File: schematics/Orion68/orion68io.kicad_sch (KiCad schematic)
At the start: 0 parts

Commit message: Schematics update
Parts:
- added C1: 100uF, symbol Device:C_Polarized
- added D5: LED, symbol Device:LED
- added J10: Euro96pin, ConnPdSilva:conn_euro96, symbol ConnPdSilva:ConnEuro96
- added J200: DB25_Socket, symbol Connector:DB25_Socket
- added J6: IDE, symbol Connector_Generic:Conn_02x20_Odd_Even
- added J7: sdcard, symbol Connector_Generic:Conn_01x06
- added J8: RTC, symbol Connector_Generic:Conn_01x06
- added LS1: Speaker, symbol Device:Speaker
- added Q4: NPN, symbol Simulation_SPICE:NPN
- added R17, R20, R21, R22, R23, R24, R25, R26, R27, R28, R29, R30, R31: 1k, symbol Device:R
- added R18, R19: 4k7, symbol Device:R
- added R32: 1K, symbol Device:R
- added R33: 47R, symbol Device:R
- added U14: 8253, Package_DIP:DIP-24_W15.24mm, symbol Timer:8253
- added U15: Multio, symbol pdSilva:Raspi pi pico
- added U16, U17: 74HC245, symbol 74xx:74HC245
- added U200: GAL16V8, symbol Logic_Programmable:GAL16V8
- added U200: PAL20RS10, Package_DIP:DIP-24_W7.62mm, symbol Logic_Programmable:PAL20RS10
- added U201: 82C55A, Package_DIP:DIP-40_W15.24mm, symbol Interface:82C55A
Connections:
- new net: U15.1 (GP0), U16.2 (A0)
- new net: U15.10 (GP7), U16.9 (A7)
- new net: U15.11 (GP8), U17.2 (A0)
- new net: U15.12 (GP9), U17.3 (A1)
- new net: U15.14 (GP10), U17.4 (A2)
- new net: U15.15 (GP11), U17.5 (A3)
- new net: U15.2 (GP1), U16.3 (A1)
- new net: U15.4 (GP2), U16.4 (A2)
- new net: U15.5 (GP3), U16.5 (A3)
- new net: U15.6 (GP4), U16.6 (A4)
- new net: U15.7 (GP5), U16.7 (A5)
- new net: U15.9 (GP6), U16.8 (A6)
- new net: C1.1, Q4.1 (C), R33.2
- new net: C1.2, LS1.1
- new net: R31.2, U17.15 (B3)
- new net: R21.2, U16.17 (B1)
- new net: D5.1 (K), R17.1
- new net: Q4.2 (B), R32.2
- new net: R30.2, U17.16 (B2)
- new net: R29.2, U17.17 (B1)
- new net: R24.2, U16.14 (B4)
- new net: R27.2, U16.11 (B7)
- new net: R20.2, U16.18 (B0)
- new net: R22.2, U16.16 (B2)
- new net: R28.2, U17.18 (B0)
- new net: R26.2, U16.12 (B6)
- new net: R25.2, U16.13 (B5)
- new net: R23.2, U16.15 (B3)
- new net +12V: J10.92
- new net +5V: D5.2 (A), J10.1, J10.33, J10.65, J6.38 (Pin_38), J7.2 (Pin_2), R18.1, R19.1, R33.1, U14.24 (VCC), U200.20 (VCC), U200.24 (VCC), U201.26 (VCC)
- new net -5V: J10.94
- new net 3V3_from_sdcard: U15.39 (VSYS), U16.20 (VCC), U17.20 (VCC)
- new net ALE: J10.73
- new net BA0: J10.18
- new net BA06: U200.1 (I1/CLK), U200.2 (I0)
- new net BA07: U200.2 (I2), U200.3 (I1)
- new net BA08: U200.3 (I3), U200.4 (I2)
- new net BA09: U200.4 (I4), U200.5 (I3)
- new net BA0A: U200.5 (I5), U200.6 (I4)
- new net BA0B: U200.6 (I6), U200.7 (I5)
- new net BA1: J10.19, J6.35 (Pin_35), R28.1, U14.19 (A0), U201.9 (A0)
- new net BA10: J10.28
- new net BA11: J10.29
- new net BA12: J10.30
- new net BA13: J10.31
- new net BA14: J10.63
- new net BA15: J10.62
- new net BA16: J10.61
- new net BA17: J10.60
- new net BA18: J10.59
- new net BA19: J10.58
- new net BA2: J10.20, J6.33 (Pin_33), R29.1, U14.20 (A1), U201.8 (A1)
- new net BA20: J10.57
- new net BA21: J10.56
- new net BA22: J10.55
- new net BA23: J10.54
- new net BA3: J10.21, J6.36 (Pin_36), R30.1
- new net BA4: J10.22, R31.1
- new net BA5: J10.23
- new net BA6: J10.24
- new net BA7: J10.25
- new net BA8: J10.26
- new net BA9: J10.27
- new net BD0: J10.2, J6.4 (Pin_4), R20.1, U14.8 (D0), U201.34 (D0)
- new net BD1: J10.3, J6.6 (Pin_6), R21.1, U14.7 (D1), U201.33 (D1)
- new net BD10: J10.12, J6.7 (Pin_7)
- new net BD11: J10.13, J6.9 (Pin_9)
- new net BD12: J10.14, J6.11 (Pin_11)
- new net BD13: J10.15, J6.13 (Pin_13)
- new net BD14: J10.16, J6.15 (Pin_15)
- new net BD15: J10.17, J6.17 (Pin_17)
- new net BD2: J10.4, J6.8 (Pin_8), R22.1, U14.6 (D2), U201.32 (D2)
- new net BD3: J10.5, J6.10 (Pin_10), R23.1, U14.5 (D3), U201.31 (D3)
- new net BD4: J10.6, J6.12 (Pin_12), R24.1, U14.4 (D4), U201.30 (D4)
- new net BD5: J10.7, J6.14 (Pin_14), R25.1, U14.3 (D5), U201.29 (D5)
- new net BD6: J10.8, J6.16 (Pin_16), R26.1, U14.2 (D6), U201.28 (D6)
- new net BD7: J10.9, J6.18 (Pin_18), R27.1, U14.1 (D7), U201.27 (D7)
- new net BD8: J10.10, J6.3 (Pin_3)
- new net BD9: J10.11, J6.5 (Pin_5)
- new net BOOTIN: J10.87
- new net BUSY: J200.11, U201.15 (PC1)
- new net B/cpurd: J10.45, J6.25 (Pin_25), U14.22 (~{RD}), U200.1 (CLK), U200.12 (IO8), U201.5 (~{RD})
- new net B/cpurw: J10.46, J6.23 (Pin_23), U14.23 (~{WR}), U200.13 (IO7), U200.13 (~{OE}), U201.36 (~{WR})
- new net CPU_CLK: J10.81
- new net CRUCLK: J10.35
- new net CRUIN: J10.36
- new net CRUOUT: J10.37
- new net CS: J7.6 (Pin_6), U15.22 (GP17)
- new net CS_82C55: U201.6 (~{CS})
- new net CS_TIMER: U14.21 (~{CS})
- new net D0: J200.2, U201.4 (PA0)
- new net D1: J200.3, U201.3 (PA1)
- new net D2: J200.4, U201.2 (PA2)
- new net D3: J200.5, U201.1 (PA3)
- new net D4: J200.6, U201.40 (PA4)
- new net D5: J200.7, U201.39 (PA5)
- new net D6: J200.8, U201.38 (PA6)
- new net D7: J200.9, U201.37 (PA7)
- new net DBIN: J10.38
- new net DMARQ: J6.21 (Pin_21)
- new net DS: J8.2 (Pin_2)
- new net DT/R: J10.75
- new net E: J10.34
- new net GND: J10.32, J10.64, J10.93, J10.95, J10.96, J200.18 (P18), J200.19 (P19), J200.20 (P20), J200.21 (P21), J200.22 (P22), J200.23 (P23), J200.24 (P24), J200.25 (P25), J6.19 (Pin_19), J6.2 (Pin_2), J6.22 (Pin_22), J6.24 (Pin_24), J6.26 (Pin_26), J6.28 (Pin_28), J6.30 (Pin_30), J6.40 (Pin_40), J7.1 (Pin_1), J8.6 (Pin_6), LS1.2, Q4.3 (E), U14.12 (GND), U15.13 (GND), U15.18 (GND), U15.23 (GND), U15.28 (GND), U15.3 (GND), U15.33 (GND), U15.38 (GND), U15.8 (GND), U16.1 (A->B), U16.10 (GND), U16.19 (CE), U17.1 (A->B), U17.10 (GND), U17.11 (B7), U17.12 (B6), U17.13 (B5), U17.14 (B4), U17.19 (CE), U200.10 (GND), U200.12 (GND), U201.7 (GND)
- new net HLDA: J10.52
- new net IAQ: J10.39
- new net IC3: J10.47
- new net INTRQ: J6.31 (Pin_31)
- new net IORDY: J6.27 (Pin_27)
- new net IRQ2: J10.48
- new net IRQ3: J10.49
- new net IRQ4: J10.50
- new net IRQ5: J10.89
- new net IRQ6: J10.90
- new net IRQ7: J10.91
- new net MISO: J7.3 (Pin_3), U15.21 (GP16)
- new net MOSI: J7.4 (Pin_4), U15.25 (GP19)
- new net M/IO: J10.76
- new net NMI: J10.41
- new net PWR_GOOD: J10.88
- new net RDY: J10.44
- new net RESET: J10.67, U201.35 (RESET)
- new net Res9: J10.69
- new net SCK: J7.5 (Pin_5), U15.24 (GP18)
- new net SCL: J8.3 (Pin_3), R18.2, U15.32 (GP27)
- new net SDA: J8.4 (Pin_4), R19.2, U15.31 (GP26)
- new net SQ: J8.1 (Pin_1)
- new net STROBE: J200.1, U201.14 (PC0)
- new net TICK_IN: J10.86, U15.34 (GP28)
- new net Vcc: J8.5 (Pin_5)
- new net audio: R32.1, U15.29 (GP22)
- new net /AS: J10.43
- new net /BAS: U200.7 (I7), U200.8 (I6)
- new net /BERR: J10.68
- new net /BLDS: U200.8 (I8), U200.9 (I7)
- new net /BUDS: U200.10 (I8), U200.9 (I9)
- new net /CS_82C55: U200.19 (IO1), U200.23 (O0)
- new net /CS_IDE: J6.37 (Pin_37), U200.18 (IO2), U200.22 (O1)
- new net /CS_MULTIO: U15.26 (GP20), U200.15 (IO5)
- new net /CS_RTC: U200.17 (I03), U200.21 (O2)
- new net /CS_SDCARD: U200.19 (O4)
- new net /CS_TIMER: U200.16 (IO4), U200.20 (O3)
- new net /DASP: J6.39 (Pin_39), R17.2
- new net /DEN: J10.74
- new net /DMACK: J6.29 (Pin_29)
- new net /HALT: J10.53
- new net /HOLD: J10.42
- new net /INTA: J10.72
- new net /INTR: J10.40
- new net /IOCS16: J6.32 (Pin_32)
- new net /IO_CS: J10.85, U200.11 (I10/~{OE}), U200.11 (I9)
- new net /LDS: J10.70
- new net /M1: J10.79
- new net /PDIAG: J6.34 (Pin_34)
- new net /RD: U15.17 (GP13)
- new net /RESET: J10.66, J6.1 (Pin_1)
- new net /RFSH: J10.80
- new net /RST: J10.51
- new net /SSO: J10.77
- new net /UDS: J10.71
- new net /WAIT: J10.78
- new net /WR: U15.16 (GP12)
- no-connect marks 0 -> 6
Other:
- note added: "+-----------------------------+-------------------+ |Sinal SPI,SPI0 (Opção Padrão)|SPI1 (Opção Padrão)| |RX (MISO),GP16 (Pino 21) |GP12 (Pino 16) | |CSn (CS), GP17 (Pino 22) |GP13 (Pino 17) | |SCK (CLK), GP18 (Pino 24) |GP14 (Pino 19) | |TX (MOSI),GP19 (Pino 25) |GP15 (Pino 20) | +-----------------------------+-------------------+"
- note added: "0xF00040-0xF0007F -> 82C55 0xF00080-0xF000BF -> IDE 0xF000C0-0xF000FF -> RTC 0xF00140-0xF0017F -> TIMER 0xF00180-0xF001BF -> SDCARD 0xF001C0-0xF001FF -> free 0xF00240-0xF0027F -> free 0xF00280-0xF002BF -> free 0xF002C0-0xF002FF -> free 0xF00340-0xF0037F -> free"
- note added: "DB25 fêmea +-------+--------------+--------------+---------------------------------------------+ |Pino |,Nome |,Direção (PC) |,Função | +-------+--------------+--------------+---------------------------------------------+ |1 |,Strobe |,Saída |,Indica que os dados são válidos (Ativo em 0)| |2 |,D0 |,E/S |,Bit de Dados 0 (LSB) | |3 |,D1 |,E/S |,Bit de Dados 1 | |4 |,D2 |,E/S |,Bit de Dados 2 | |5 |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"

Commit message: Schematics update
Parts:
- U15: footprint (none) -> Package_DIP:DIP-40_W15.24mm
- renumbered U200 to U9999
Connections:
- net /CS_SDCARD: now also U200.14 (IO6); no longer U9999.19 (O4)
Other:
- moved on the sheet: U9999
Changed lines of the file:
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@@
 	)
 	(label "BA0A"
-		(at 64.77 254 180)
+		(at 66.04 311.15 180)
 		(effects
 			(font
@@
 	)
 	(label "{slash}BLDS"
-		(at 64.77 261.62 180)
+		(at 66.04 318.77 180)
 		(effects
 			(font
@@
 	)
 	(label "{slash}IO_CS"
-		(at 64.77 266.7 180)
+		(at 66.04 323.85 180)
 		(effects
 			(font
@@
 	)
 	(label "{slash}BAS"
-		(at 64.77 259.08 180)
+		(at 66.04 316.23 180)
 		(effects
 			(font
@@
 	)
 	(label "{slash}CS_IDE"
-		(at 90.17 246.38 0)
+		(at 91.44 303.53 0)
 		(effects
 			(font
@@
 	)
 	(label "BA09"
-		(at 64.77 251.46 180)
+		(at 66.04 308.61 180)
 		(effects
 			(font
@@
 	)
 	(label "BA0B"
-		(at 64.77 256.54 180)
+		(at 66.04 313.69 180)
 		(effects
 			(font
@@
 	)
 	(label "BA07"
-		(at 64.77 246.38 180)
+		(at 66.04 303.53 180)
 		(effects
 			(font
@@
 	)
 	(label "{slash}BUDS"
-		(at 64.77 264.16 180)
+		(at 66.04 321.31 180)
 		(effects
 			(font
@@
 	)
 	(label "BA08"
-		(at 64.77 248.92 180)
+		(at 66.04 306.07 180)
 		(effects
 			(font
@@
 	)
 	(label "{slash}CS_SDCARD"
-		(at 90.17 254 0)
+		(at 45.72 260.35 0)
 		(effects
 			(font
@@
 	)
 	(label "BA06"
-		(at 64.77 243.84 180)
+		(at 66.04 300.99 180)
 		(effects
 			(font
@@
 	)
 	(label "{slash}CS_RTC"
-		(at 90.17 248.92 0)
+		(at 91.44 306.07 0)
 		(effects
 			(font
@@
 	)
 	(label "B{slash}cpurw"
-		(at 64.77 274.32 180)
+		(at 66.04 331.47 180)
 		(effects
 			(font
@@
 	)
 	(label "B{slash}cpurd"
-		(at 64.77 271.78 180)
+		(at 66.04 328.93 180)
 		(effects
 			(font
@@
 	)
 	(label "{slash}CS_82C55"
-		(at 90.17 243.84 0)
+		(at 91.44 300.99 0)
 		(effects
 			(font
@@
 	)
 	(label "{slash}CS_TIMER"
-		(at 90.17 251.46 0)
+		(at 91.44 308.61 0)
 		(effects
 			(font
@@
 			)
 		)
-		(property "Footprint" ""
+		(property "Footprint" "Package_DIP:DIP-40_W15.24mm"
 			(at 199.39 104.14 0)
 			(effects
@@
 	(symbol
 		(lib_id "power:GND")
-		(at 77.47 279.4 0)
+		(at 78.74 336.55 0)
 		(unit 1)
 		(exclude_from_sim no)
@@
 		(fields_autoplaced yes)
 		(property "Reference" "#PWR085"
-			(at 77.47 285.75 0)
+			(at 78.74 342.9 0)
 			(effects
 				(font
@@
 		)
 		(property "Value" "GND"
-			(at 77.47 284.48 0)
+			(at 78.74 341.63 0)
 			(effects
 				(font
@@
 		)
 		(property "Footprint" ""
-			(at 77.47 279.4 0)
+			(at 78.74 336.55 0)
 			(effects
 				(font
@@
 		)
 		(property "Datasheet" ""
-			(at 77.47 279.4 0)
+			(at 78.74 336.55 0)
 			(effects
 				(font
@@
 		)
 		(property "Description" "Power symbol creates a global label with name \"GND\" , ground"
-			(at 77.47 279.4 0)
+			(at 78.74 336.55 0)
 			(effects
 				(font
@@
 	(symbol
 		(lib_id "power:+5V")
-		(at 77.47 238.76 0)
+		(at 78.74 295.91 0)
 		(unit 1)
 		(exclude_from_sim no)
@@
 		(fields_autoplaced yes)
 		(property "Reference" "#PWR090"
-			(at 77.47 242.57 0)
+			(at 78.74 299.72 0)
 			(effects
 				(font
@@
 		)
 		(property "Value" "+5V"
-			(at 77.47 233.68 0)
+			(at 78.74 290.83 0)
 			(effects
 				(font
@@
 		)
 		(property "Footprint" ""
-			(at 77.47 238.76 0)
+			(at 78.74 295.91 0)
 			(effects
 				(font
@@
 		)
 		(property "Datasheet" ""
-			(at 77.47 238.76 0)
+			(at 78.74 295.91 0)
 			(effects
 				(font
@@
 		)
 		(property "Description" "Power symbol creates a global label with name \"+5V\""
-			(at 77.47 238.76 0)
+			(at 78.74 295.91 0)
 			(effects
 				(font
@@
 	(symbol
 		(lib_id "Logic_Programmable:PAL20RS10")
-		(at 77.47 259.08 0)
+		(at 78.74 316.23 0)
 		(unit 1)
 		(exclude_from_sim no)
@@
 		(dnp no)
 		(fields_autoplaced yes)
-		(property "Reference" "U200"
-			(at 79.6133 237.49 0)
+		(property "Reference" "U9999"
+			(at 80.8833 294.64 0)
 			(effects
 				(font
@@
 		)
 		(property "Value" "PAL20RS10"
-			(at 79.6133 240.03 0)
+			(at 80.8833 297.18 0)
 			(effects
 				(font
@@
 		)
 		(property "Footprint" "Package_DIP:DIP-24_W7.62mm"
-			(at 77.47 259.08 0)
+			(at 78.74 316.23 0)
 			(effects
 				(font
@@
 		)
 		(property "Datasheet" ""
-			(at 77.47 259.08 0)
+			(at 78.74 316.23 0)
 			(effects
 				(font
@@
 		)
 		(property "Description" "Programmable Logic Array, DIP-24 (Narrow)"
-			(at 77.47 259.08 0)
+			(at 78.74 316.23 0)
 			(effects
 				(font
@@
 			(project "Orion68"
 				(path "/c7ab032b-c937-44de-ab42-c91dee57f0a8/a3cb64b8-9a58-4dca-a498-ee5e38308bd0"
-					(reference "U200")
+					(reference "U9999")
 					(unit 1)
 				)

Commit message: Updating
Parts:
- removed U14: 8253, Package_DIP:DIP-24_W15.24mm, symbol Timer:8253
- removed U9999: PAL20RS10, Package_DIP:DIP-24_W7.62mm, symbol Logic_Programmable:PAL20RS10
- added R212: 1k, Resistor_THT:R_Axial_DIN0204_L3.6mm_D1.6mm_P5.08mm_Horizontal, symbol Device:R
- C_S400: renamed from C1; footprint (none) -> Capacitor_THT:CP_Radial_D5.0mm_P2.50mm
- D_S300: renamed from D5; footprint (none) -> Diode_THT:D_T-1_P5.08mm_Horizontal
- J_S100: renamed from J200; footprint (none) -> Connector_PinHeader_2.54mm:PinHeader_2x13_P2.54mm_Vertical
- J_S200: renamed from J7; footprint (none) -> Connector_PinSocket_2.54mm:PinSocket_1x06_P2.54mm_Vertical
- J_S201: renamed from J8; footprint (none) -> Connector_PinSocket_2.54mm:PinSocket_1x06_P2.54mm_Vertical
- J_S300: renamed from J6; footprint (none) -> Connector_PinHeader_2.54mm:PinHeader_2x20_P2.54mm_Horizontal
- LS_S400: renamed from LS1; footprint (none) -> Connector_PinHeader_2.54mm:PinHeader_1x02_P2.54mm_Vertical
- Q_S400: renamed from Q4; footprint (none) -> Package_TO_SOT_THT:TO-92L_Inline
- R200: renamed from R20; footprint (none) -> Resistor_THT:R_Axial_DIN0204_L3.6mm_D1.6mm_P5.08mm_Horizontal
- R201: renamed from R21; footprint (none) -> Resistor_THT:R_Axial_DIN0204_L3.6mm_D1.6mm_P5.08mm_Horizontal
- R202: renamed from R22; footprint (none) -> Resistor_THT:R_Axial_DIN0204_L3.6mm_D1.6mm_P5.08mm_Horizontal
- R203: renamed from R23; footprint (none) -> Resistor_THT:R_Axial_DIN0204_L3.6mm_D1.6mm_P5.08mm_Horizontal
- R204: renamed from R24; footprint (none) -> Resistor_THT:R_Axial_DIN0204_L3.6mm_D1.6mm_P5.08mm_Horizontal
- R205: renamed from R25; footprint (none) -> Resistor_THT:R_Axial_DIN0204_L3.6mm_D1.6mm_P5.08mm_Horizontal
- R206: renamed from R26; footprint (none) -> Resistor_THT:R_Axial_DIN0204_L3.6mm_D1.6mm_P5.08mm_Horizontal
- R207: renamed from R27; footprint (none) -> Resistor_THT:R_Axial_DIN0204_L3.6mm_D1.6mm_P5.08mm_Horizontal
- R208: renamed from R28; footprint (none) -> Resistor_THT:R_Axial_DIN0204_L3.6mm_D1.6mm_P5.08mm_Horizontal
- R209: renamed from R29; footprint (none) -> Resistor_THT:R_Axial_DIN0204_L3.6mm_D1.6mm_P5.08mm_Horizontal
- R210: renamed from R30; footprint (none) -> Resistor_THT:R_Axial_DIN0204_L3.6mm_D1.6mm_P5.08mm_Horizontal
- R211: renamed from R31; footprint (none) -> Resistor_THT:R_Axial_DIN0204_L3.6mm_D1.6mm_P5.08mm_Horizontal
- R213: renamed from R18; footprint (none) -> Resistor_THT:R_Axial_DIN0204_L3.6mm_D1.6mm_P5.08mm_Horizontal
- R214: renamed from R19; footprint (none) -> Resistor_THT:R_Axial_DIN0204_L3.6mm_D1.6mm_P5.08mm_Horizontal
- R_S300: renamed from R17; footprint (none) -> Resistor_THT:R_Axial_DIN0204_L3.6mm_D1.6mm_P5.08mm_Horizontal
- R_S400: renamed from R33; footprint (none) -> Resistor_THT:R_Axial_DIN0204_L3.6mm_D1.6mm_P5.08mm_Horizontal
- R_S401: renamed from R32; footprint (none) -> Resistor_THT:R_Axial_DIN0204_L3.6mm_D1.6mm_P5.08mm_Horizontal
- U200: footprint (none) -> Package_DIP:DIP-20_W7.62mm
- U_S201: renamed from U16; footprint (none) -> Package_DIP:DIP-20_W7.62mm
- U_S202: renamed from U17; footprint (none) -> Package_DIP:DIP-20_W7.62mm
- renumbered J10 to J200, U201 to U_S100, U15 to U_S200
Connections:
- net BA5: now also R212.1
- net GND: no longer U_S202.14 (B4)
- new net: R212.2, U_S202.14 (B4)
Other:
- note added: "+---------+-----+---------+------------+ |Binário | LDS | Ender. |D0-D7 (LDS)| |A5...A1 | A0 | Decimal |D8-D15 (UDS)| +---------+-----+---------+------------+ |00000 | 0 | 0(Par) | LDS | |00000 | 1 | 1(Ímpar)| UDS | |00001 | 0 | 2(Par) | LDS | |00001 | 1 | 3(Ímpar)| UDS | |00010 | 0 | 4(Par) | LDS | |00010 | 1 | 5(Ímpar)| UDS | |00011 | 0 | 6(Par) | LDS | |00011 | 1 | 7(Ímpar)| UDS | |00100 | 0 |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"
- note added: "0xF00040-0xF0007F -> 82C55 0xF00080-0xF000BF -> IDE 0xF000C0-0xF000FF -> RTC 0xF00140-0xF0017F -> TIMER 0xF00180-0xF001BF -> SDCARD 0xF001C0-0xF001FF -> free 0xF00240-0xF0027F -> free 0xF00280-0xF002BF -> free 0xF002C0-0xF002FF -> free 0xF00340-0xF0037F -> free 0xFB8000-0xFB803F -> VGA-CARD"
- note added: "IO board - 200"
- note added: "Setor S100"
- note added: "Setor S200"
- note added: "Setor S300"
- note added: "Setor S4 00"
- note removed: "0xF00040-0xF0007F -> 82C55 0xF00080-0xF000BF -> IDE 0xF000C0-0xF000FF -> RTC 0xF00140-0xF0017F -> TIMER 0xF00180-0xF001BF -> SDCARD 0xF001C0-0xF001FF -> free 0xF00240-0xF0027F -> free 0xF00280-0xF002BF -> free 0xF002C0-0xF002FF -> free 0xF00340-0xF0037F -> free"
- note removed: "IO board"
- moved on the sheet: J_S200, J_S201

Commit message: Schematic verified to board
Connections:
- net BA0A is gone; now on net BA10: U200.5 (I5)
- net BA0B is gone; now on net BA11: U200.6 (I6)
- net B/cpurw: no longer J200.46
- net /RAM_CS: now reaches J200.84
- net /AS renamed B/AS
- net /LDS renamed B/LDS
- net /UDS renamed B/UDS
- new net B/cpuwr: J200.46

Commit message: Cpu board fixed and running
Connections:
- net /IO_CS: no longer J200.85
- net /RAM_CS: no longer names the net of J200.84
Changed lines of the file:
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@@
-		)
-	)
-	(label "{slash}IO_CS"
-		(at 389.89 133.35 0)
-		(effects
-			(font
-				(size 1.27 1.27)
-			)
-			(justify left bottom)
 		)
 	)
@@
 			)
 			(justify left bottom)
-		)
-	)
-	(label "{slash}RAM_CS"
-		(at 389.89 130.81 0)
-		(effects
-			(font
-				(size 1.27 1.27)
-			)
-			(justify left bottom)

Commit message: Updating...
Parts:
- renumbered D_S300 to D_S500, J_S300 to J_S500, R_S300 to R_S500
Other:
- note added: "Setor S400"
- note added: "Setor S500"
- note removed: "Setor S300"
- note removed: "Setor S4 00"
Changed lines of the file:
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@@
 		)
 	)
-	(text "Setor S4\n00"
+	(text "Setor S400"
 		(exclude_from_sim no)
 		(at 125.73 204.216 0)
@@
 		)
 	)
-	(text "Setor S300"
+	(text "Setor S500"
 		(exclude_from_sim no)
 		(at 217.932 205.232 0)
@@
 		(dnp no)
 		(fields_autoplaced yes)
-		(property "Reference" "D_S300"
+		(property "Reference" "D_S500"
 			(at 290.83 258.1274 90)
 			(effects
@@
 			(project "Orion68"
 				(path "/c7ab032b-c937-44de-ab42-c91dee57f0a8/a3cb64b8-9a58-4dca-a498-ee5e38308bd0"
-					(reference "D_S300")
+					(reference "D_S500")
 					(unit 1)
 				)
@@
 		(dnp no)
 		(fields_autoplaced yes)
-		(property "Reference" "J_S300"
+		(property "Reference" "J_S500"
 			(at 255.27 201.93 0)
 			(effects
@@
 			(project "Orion68"
 				(path "/c7ab032b-c937-44de-ab42-c91dee57f0a8/a3cb64b8-9a58-4dca-a498-ee5e38308bd0"
-					(reference "J_S300")
+					(reference "J_S500")
 					(unit 1)
 				)
@@
 		(dnp no)
 		(fields_autoplaced yes)
-		(property "Reference" "R_S300"
+		(property "Reference" "R_S500"
 			(at 289.56 264.1599 0)
 			(effects
@@
 			(project "Orion68"
 				(path "/c7ab032b-c937-44de-ab42-c91dee57f0a8/a3cb64b8-9a58-4dca-a498-ee5e38308bd0"
-					(reference "R_S300")
+					(reference "R_S500")
 					(unit 1)
 				)

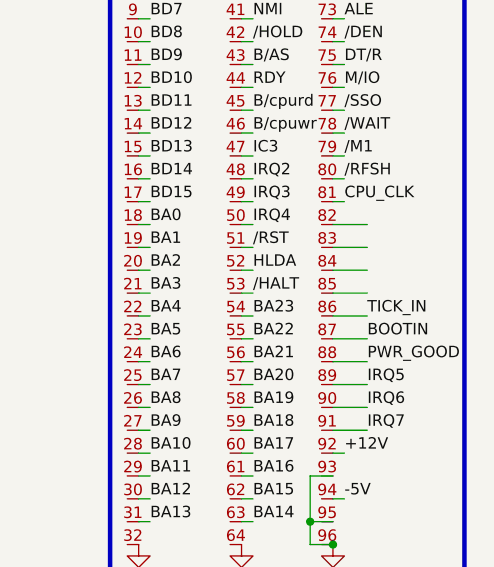
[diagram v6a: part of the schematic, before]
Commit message: A20 bug fixed, missing serial CSA, running ok
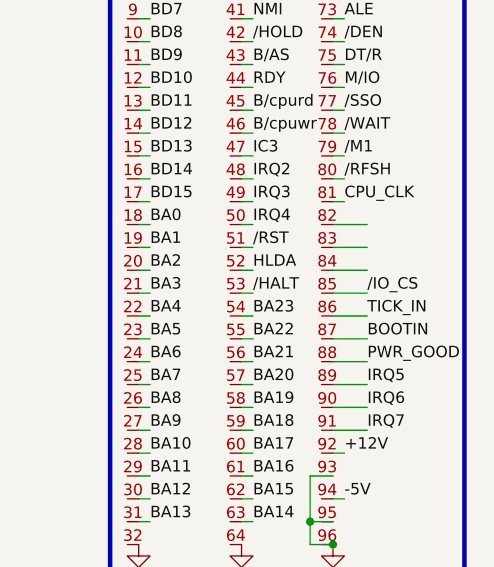
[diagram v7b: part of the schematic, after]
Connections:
- net /IO_CS: now also J200.85
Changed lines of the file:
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@@
+		)
+	)
+	(label "{slash}IO_CS"
+		(at 389.89 133.35 0)
+		(effects
+			(font
+				(size 1.27 1.27)
+			)
+			(justify left bottom)
 		)
 	)
